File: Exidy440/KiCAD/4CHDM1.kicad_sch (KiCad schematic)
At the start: 3 parts, among them P5 50 PIN RIBBON CABLE, U5J? 74LS04

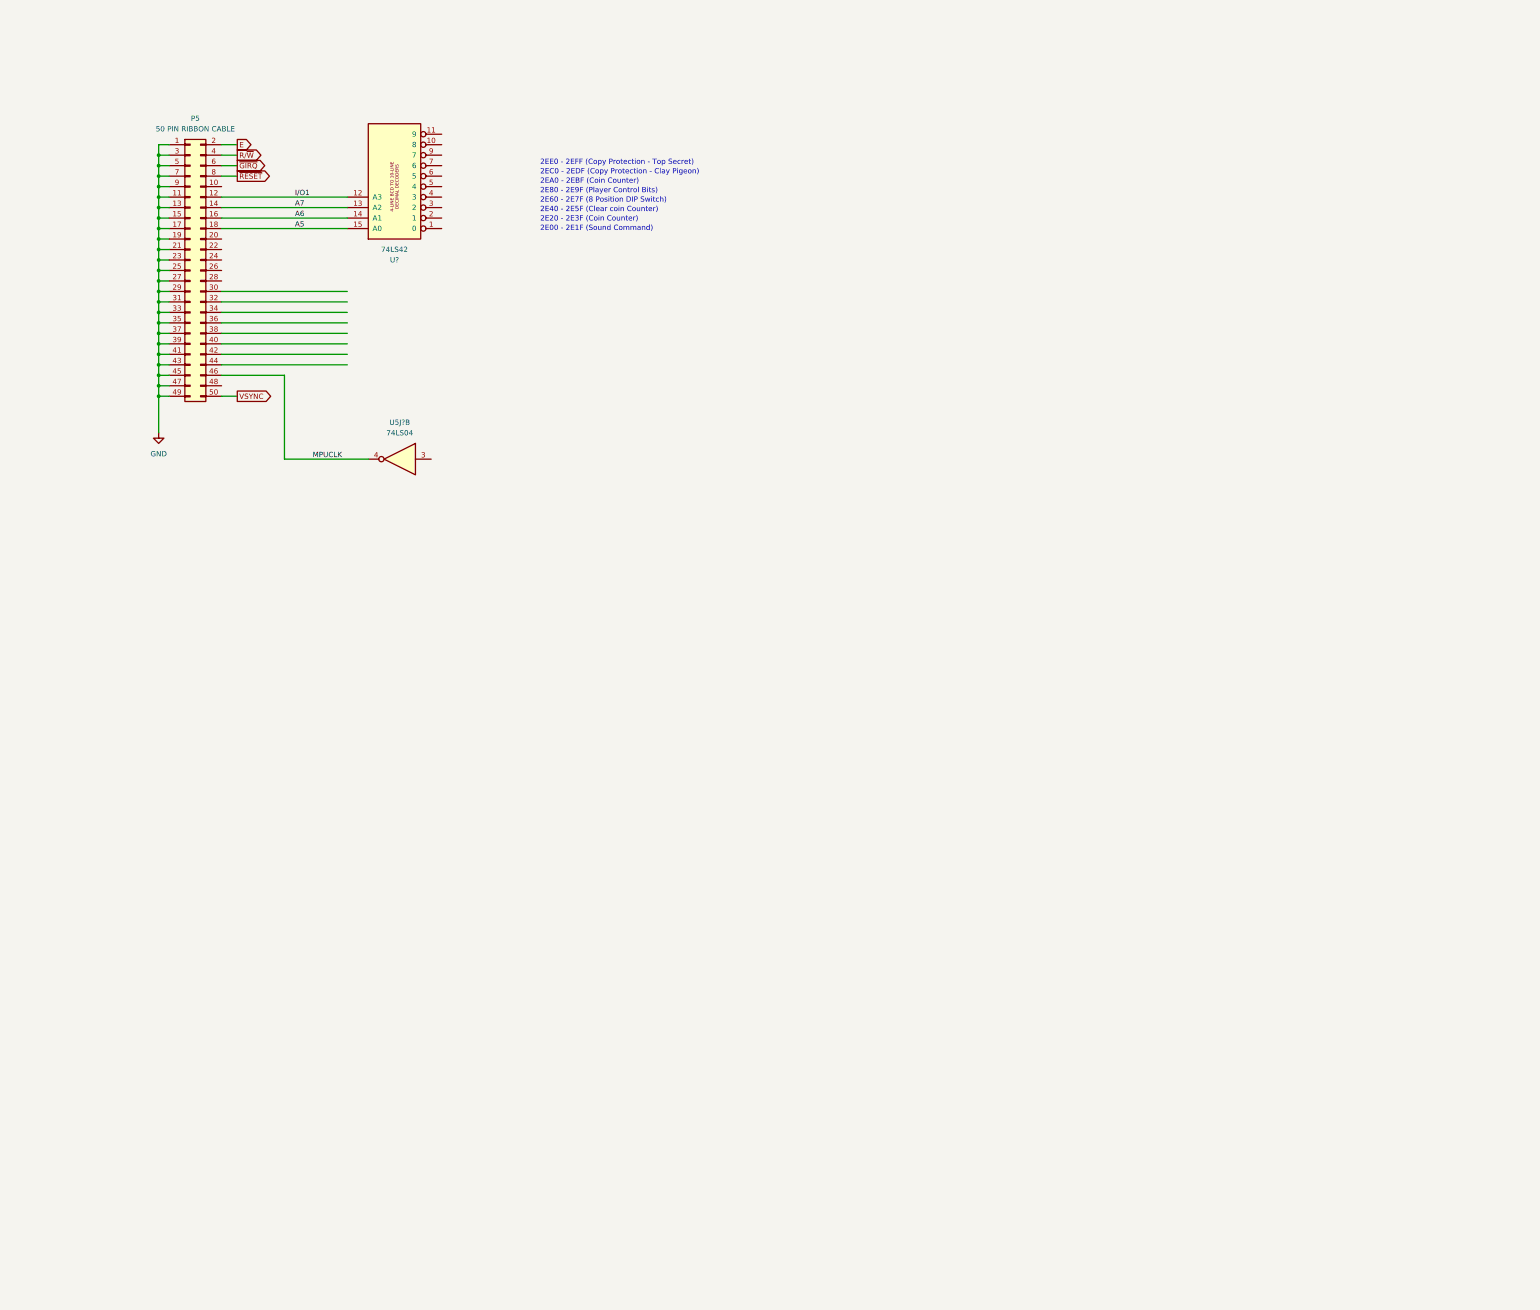
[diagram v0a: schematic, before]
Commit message: Correction of references after copy/paste issue.  Additional IO on audio board.
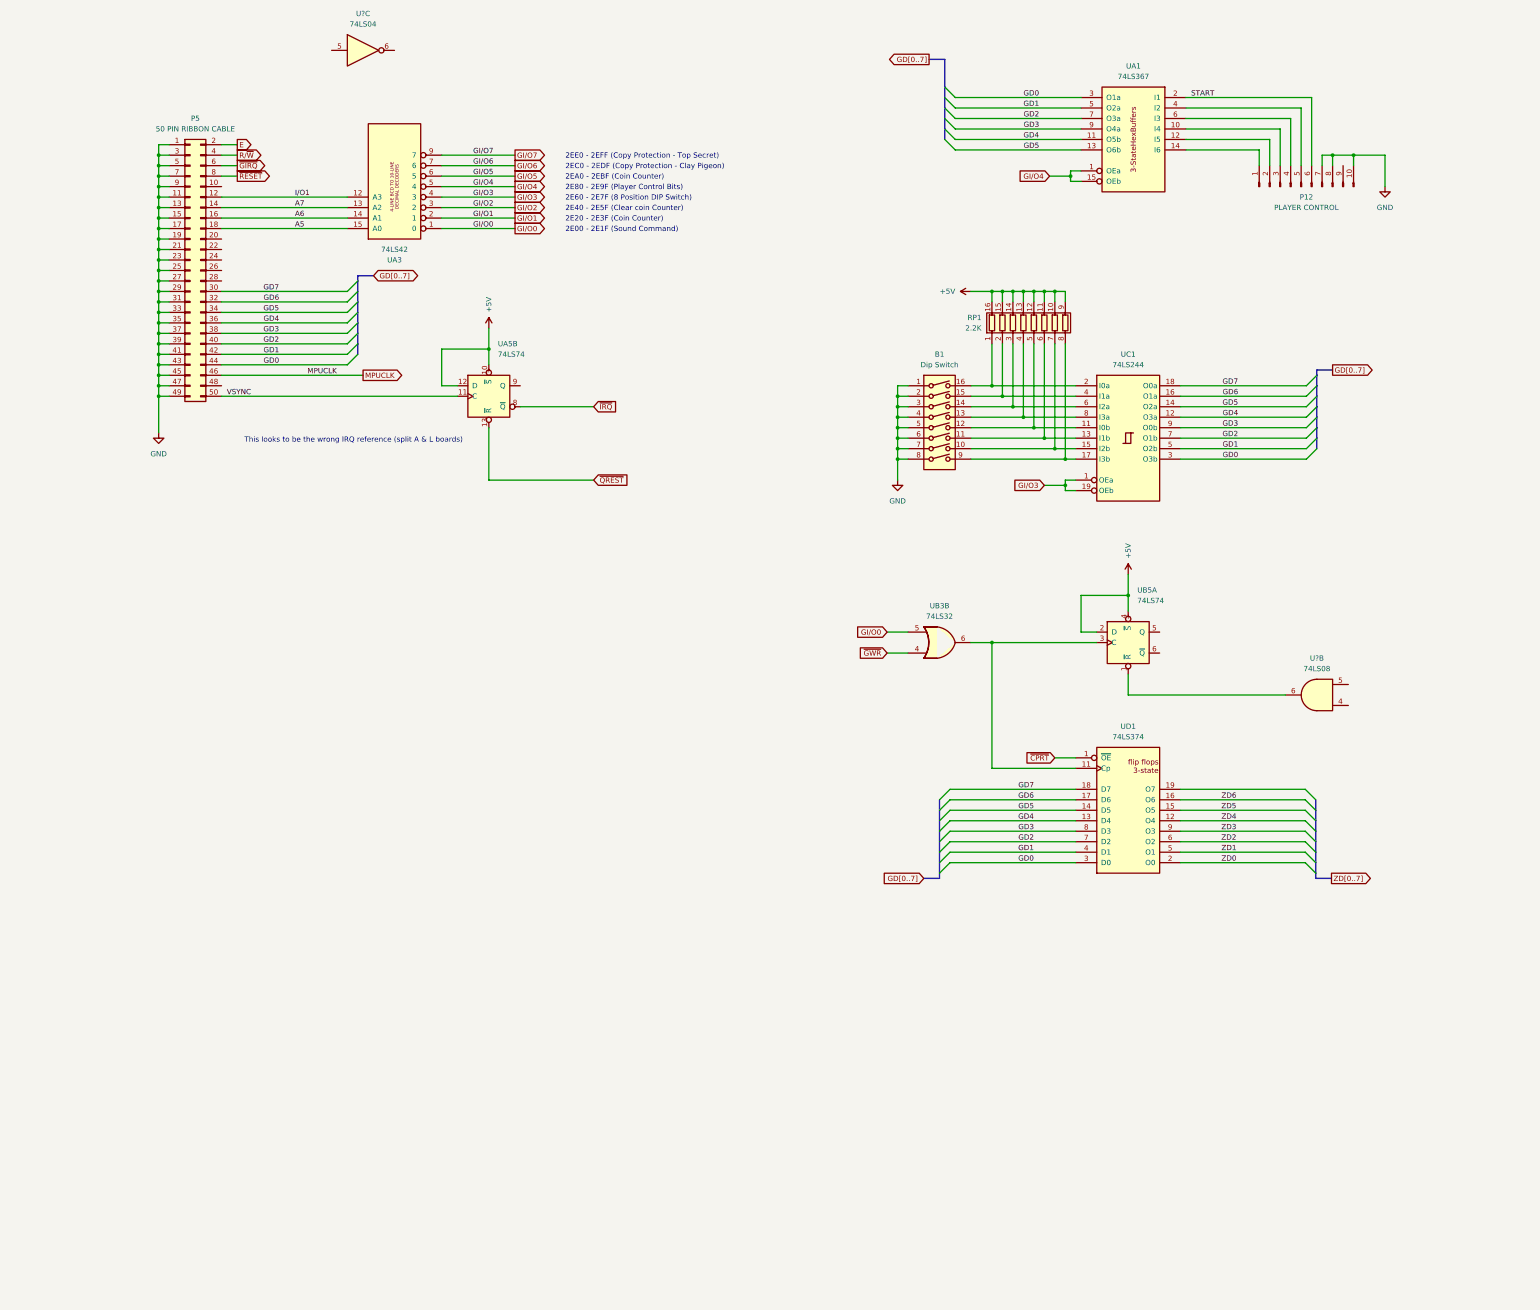
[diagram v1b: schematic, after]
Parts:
- removed U5J?: 74LS04, symbol jt74:74LS04
- added B1: Dip Switch, symbol Switch:SW_DIP_x08
- added P12: PLAYER CONTROL, symbol Connector:Conn_01x10_Pin
- added RP1: 2.2K, symbol Device:R_Pack08
- added U?: 74LS04, symbol jt74:74LS04
- added U?: 74LS08, symbol jt74:74LS08
- added UA1: 74LS367, symbol jt74:74LS367
- added UA5, UB5: 74LS74, symbol jt74:74LS74
- added UB3: 74LS32, symbol jt74:74LS32
- added UC1: 74LS244, symbol jt74:74LS244
- added UD1: 74LS374, symbol jt74:74LS374
- gave numbers to parts that had none: 1
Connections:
- net GND: now also B1.1, B1.2, B1.3, B1.4, B1.5, B1.6, B1.7, B1.8, P12.10 (Pin_10), P12.7 (Pin_7), P12.8 (Pin_8), UA1.8 (GND), UC1.10 (GND)
- net VCC: now also UA1.16 (VCC), UC1.20 (VCC)
- net VSYNC: now also UA5.11 (C)
- net GI/O0: now reaches UA3.1 (0)
- net GI/O0: now also UB3.5
- net GI/O1: now reaches UA3.2 (1)
- net GI/O2: now reaches UA3.3 (2)
- net GI/O3: now reaches UA3.4 (3)
- net GI/O3: now also UC1.1 (OEa), UC1.19 (OEb)
- net GI/O4: now reaches UA3.5 (4)
- net GI/O4: now also UA1.1 (OEa), UA1.15 (OEb)
- net GI/O5: now reaches UA3.6 (5)
- net GI/O6: now reaches UA3.7 (6)
- net GI/O7: now reaches UA3.9 (7)
- net GD7: now reaches P5.30 (Pin_30)
- net GD7: now also UC1.18 (O0a), UD1.18 (D7)
- net GD6: now reaches P5.32 (Pin_32)
- net GD6: now also UC1.16 (O1a), UD1.17 (D6)
- net GD5: now reaches P5.34 (Pin_34)
- net GD5: now also UA1.13 (O6b), UC1.14 (O2a), UD1.14 (D5)
- net GD4: now reaches P5.36 (Pin_36)
- net GD4: now also UA1.11 (O5b), UC1.12 (O3a), UD1.13 (D4)
- net GD3: now reaches P5.38 (Pin_38)
- net GD3: now also UA1.9 (O4a), UC1.9 (O0b), UD1.8 (D3)
- net GD2: now reaches P5.40 (Pin_40)
- net GD2: now also UA1.7 (O3a), UC1.7 (O1b), UD1.7 (D2)
- net GD1: now reaches P5.42 (Pin_42)
- net GD1: now also UA1.5 (O2a), UC1.5 (O2b), UD1.4 (D1)
- net GD0: now reaches P5.44 (Pin_44)
- net GD0: now also UA1.3 (O1a), UC1.3 (O3b), UD1.3 (D0)
- new net: UB3.6, UB5.3 (C), UD1.11 (Cp)
- new net: U?.6, UB5.1 (~{R})
- new net: B1.12, RP1.5 (R5.1), UC1.11 (I0b)
- new net: B1.11, RP1.6 (R6.1), UC1.13 (I1b)
- new net: B1.10, RP1.7 (R7.1), UC1.15 (I2b)
- new net: B1.9, RP1.8 (R8.1), UC1.17 (I3b)
- new net: B1.16, RP1.1 (R1.1), UC1.2 (I0a)
- new net: B1.15, RP1.2 (R2.1), UC1.4 (I1a)
- new net: B1.14, RP1.3 (R3.1), UC1.6 (I2a)
- new net: B1.13, RP1.4 (R4.1), UC1.8 (I3a)
- new net: P12.3 (Pin_3), UA1.10 (I4)
- new net: P12.2 (Pin_2), UA1.12 (I5)
- new net: P12.1 (Pin_1), UA1.14 (I6)
- new net: P12.5 (Pin_5), UA1.4 (I2)
- new net: P12.4 (Pin_4), UA1.6 (I3)
- new net +5V: RP1.10 (R7.2), RP1.11 (R6.2), RP1.12 (R5.2), RP1.13 (R4.2), RP1.14 (R3.2), RP1.15 (R2.2), RP1.16 (R1.2), RP1.9 (R8.2), UA5.10 (~{S}), UA5.12 (D), UB5.2 (D), UB5.4 (~{S})
- new net START: P12.6 (Pin_6), UA1.2 (I1)
- new net ZD0: UD1.2 (O0)
- new net ZD1: UD1.5 (O1)
- new net ZD2: UD1.6 (O2)
- new net ZD3: UD1.9 (O3)
- new net ZD4: UD1.12 (O4)
- new net ZD5: UD1.15 (O5)
- new net ZD6: UD1.16 (O6)
- new net ~{CPRT}: UD1.1 (~{OE})
- new net ~{GWR}: UB3.4
- new net ~{IRQ}: UA5.8 (~{Q})
- new net ~{QREST}: UA5.13 (~{R})
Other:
- note added: "This looks to be the wrong IRQ reference (split A & L boards)"

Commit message: Minor modifications to IO board
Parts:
- added C1: 100uF, symbol Device:C_Polarized
- added C2, C3, C4, C5: 4.7uF, symbol Device:C_Polarized
- added P21: Power Connector, symbol Connector_Generic:Conn_01x10
- added Q15: L7812, symbol Regulator_Linear:L7812
- added Q16: L7912, symbol Regulator_Linear:L7912
- added U?: 74LS42, symbol jt74:74LS42
- added unit 3 of UB3
- added UD4: 74LS07, symbol jt74:74LS07
- gave numbers to parts that had none: 2
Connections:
- net +5V: now also C1.1, P21.4 (Pin_4), P21.5 (Pin_5), P21.6 (Pin_6), P21.7 (Pin_7)
- net E: now also UE4.5
- net GND: now also C1.2, C2.2, C3.1, C4.2, C5.1, P21.1 (Pin_1), P21.10 (Pin_10), P21.2 (Pin_2), P21.9 (Pin_9), Q15.2 (GND), Q16.1 (GND), U?.8 (GND)
- net R/~{W}: now also UB3.9
- net VCC: now also U?.16 (VCC)
- net ~{CPRT}: now also UH4.4, U?.3 (2)
- net ~{GWR}: now also UB3.8
- net ~{QREST}: now also U?.7 (6)
- net at UE4.6: now also UB3.10
- net ~{CACC}: now reaches UB5.5 (Q)
- net ~{GFIRQ}: now reaches UB5.6 (~{Q})
- net ~{GRESET}: now reaches UH4.5
- net ~{GRESET}: now also UD4.8
- net ~{RESET}: no longer names the net of P5.8 (Pin_8)
- net ~{RESET}: now also UD4.9
- new net +12V: C4.1, Q15.3 (OUT)
- new net -12V: C5.2, Q16.3 (VO)
- new net VA+: C2.1, P21.3 (Pin_3), Q15.1 (IN)
- new net VA-: C3.2, P21.8 (Pin_8), Q16.2 (VI)
- new net ~{BANK}: U?.6 (5)
- new net ~{DMAC}: U?.1 (0)
- new net ~{VRAM}: U?.2 (1)
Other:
- moved on the sheet: P5, UD1, UE4C, UH4B
